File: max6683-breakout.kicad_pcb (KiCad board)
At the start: 2 copper layers, 11 parts, among them J1 Conn_01x05, J2 Conn_01x05, U1 MAX6683

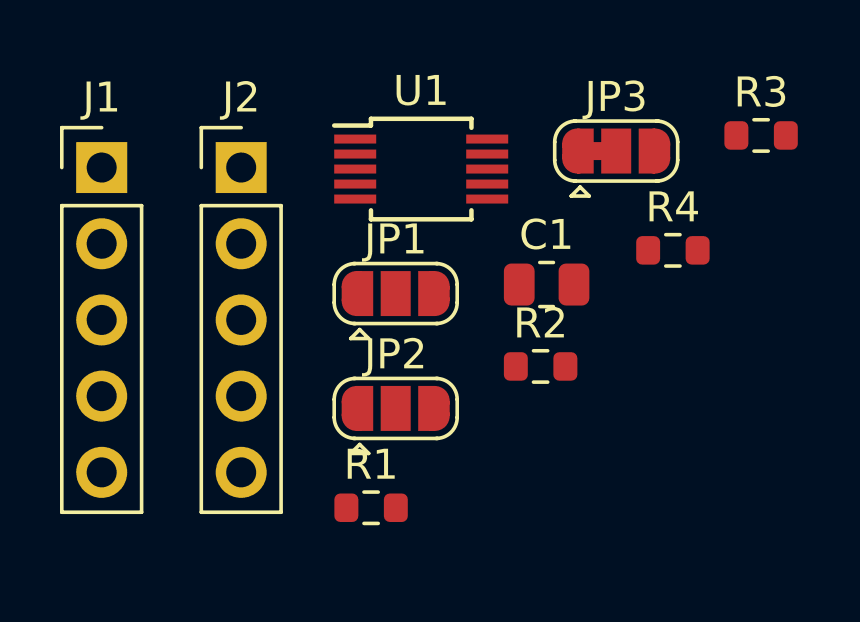
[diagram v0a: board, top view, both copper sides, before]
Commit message: Initial PCB component placement
Supports #44.
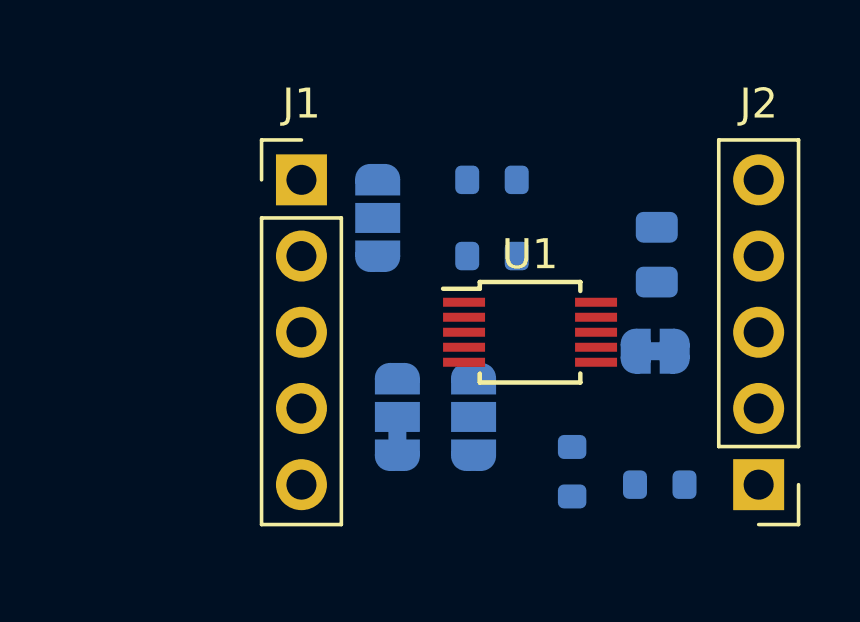
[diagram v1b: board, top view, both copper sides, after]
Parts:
- added JP4: SolderJumper_2_Bridged, Jumper:SolderJumper-2_P1.3mm_Bridged_RoundedPad1.0x1.5mm, B.Cu at (156.6, 102.2)
- C1, JP1, JP2, JP3, R3, R4: moved to B.Cu
- R1, R2: value 4.7k -> 2.2k; moved to B.Cu
- moved J2 20.2 mm to (160.0, 106.7), turned to 180 degrees
- moved R3 12.1 mm to (156.7, 106.7)
- moved R1 11.6 mm to (151.1, 96.5)
- moved JP3 11.5 mm to (148.0, 104.4), turned to 90 degrees
- moved R4 8.11 mm to (153.8, 106.2), turned to -90 degrees
- moved J1 6.67 mm to (144.8, 96.5)
- moved U1 6.54 mm to (152.4, 101.6)
- moved R2 4.02 mm to (151.1, 99.1)
- moved C1 3.80 mm to (156.6, 99.0), turned to 90 degrees
- moved JP2 2.61 mm to (150.5, 104.4), turned to -90 degrees
- moved JP1 2.59 mm to (147.3, 97.8), turned to 90 degrees
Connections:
- J2 pad 1: Net-(U1-Pad6) -> ~{ALERT}
- JP2 pad 1: Net-(JP2-Pad1) -> SCL
- JP2 pad 3: SCL -> Net-(JP2-Pad3)
- JP3 pad 1: SDA -> GND
- JP3 pad 3: GND -> SDA
- R3 pad 1: +3V3 -> Net-(JP4-Pad1)
- R3 pad 2: unconnected-(R3-Pad2) -> ~{ALERT}
- R4 pad 2: Net-(JP2-Pad1) -> Net-(JP2-Pad3)
- U1 pad 6: Net-(U1-Pad6) -> ~{ALERT}

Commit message: Add PCB outline
Parts moved for clearance and ease of routing.

Supports #44.
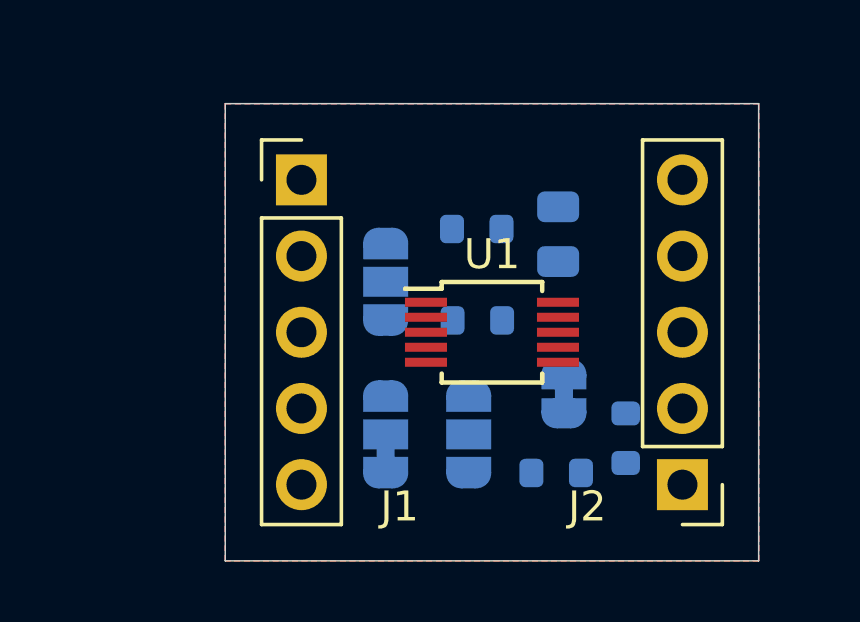
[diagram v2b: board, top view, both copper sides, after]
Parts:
- moved C1 3.36 mm to (153.3, 98.3)
- moved JP4 3.36 mm to (153.5, 103.7), turned to 90 degrees
- moved J2 2.54 mm to (157.5, 106.7)
- moved R2 2.20 mm to (150.6, 101.2)
- moved JP1 2.14 mm to (147.6, 99.9)
- moved R3 1.92 mm to (155.6, 105.1), turned to -90 degrees
- moved R1 1.72 mm to (150.6, 98.2)
- moved U1 1.27 mm to (151.1, 101.6)
- moved JP3 0.70 mm to (147.6, 105.0)
- moved JP2 0.60 mm to (150.4, 105.0)
- moved R4 0.53 mm to (153.3, 106.3), turned to 180 degrees
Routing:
- added copper zone on B.Cu, net +3V3
- added copper zone on F.Cu, net GND
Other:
- board outline added: 17.8 x 15.2 mm

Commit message: Update PCB to eliminate clearance DRC issues
Supports #44.
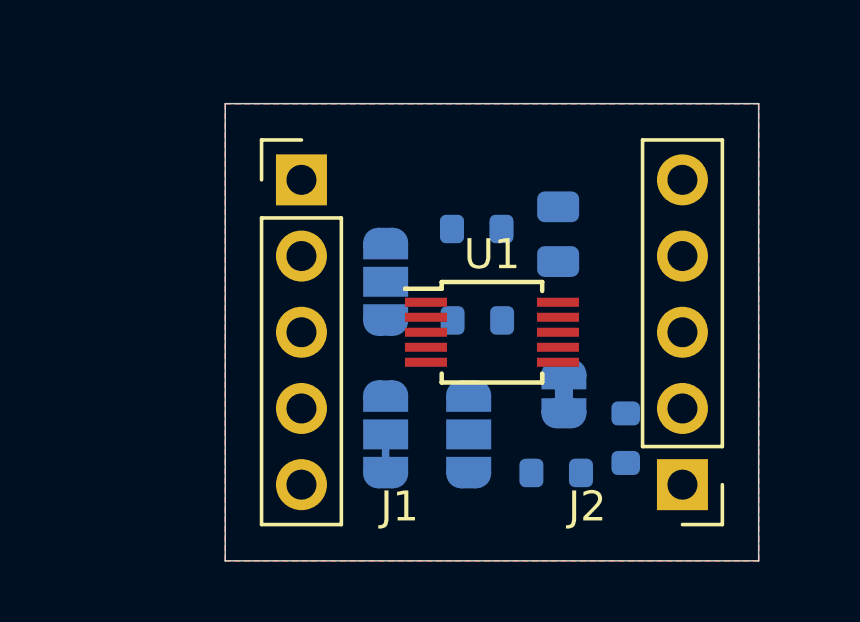
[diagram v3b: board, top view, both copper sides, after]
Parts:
- JP3: footprint Jumper:SolderJumper-3_P1.3mm_Bridged12_RoundedPad1.0x1.5mm -> Jumper:SolderJumper-3_P1.3mm_Open_RoundedPad1.0x1.5mm
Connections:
- C1 pad 2: GND -> ADD
- J1 pad 5: GND -> ADD
- JP3 pad 1: GND -> ADD
- U1 pad 5: GND -> ADD
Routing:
- net ADD: track 0.00 -> 1.30 mm
- added copper zone on F.Cu, net ADD
- removed copper zone on F.Cu, net GND

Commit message: Begin routing
Supports #44.
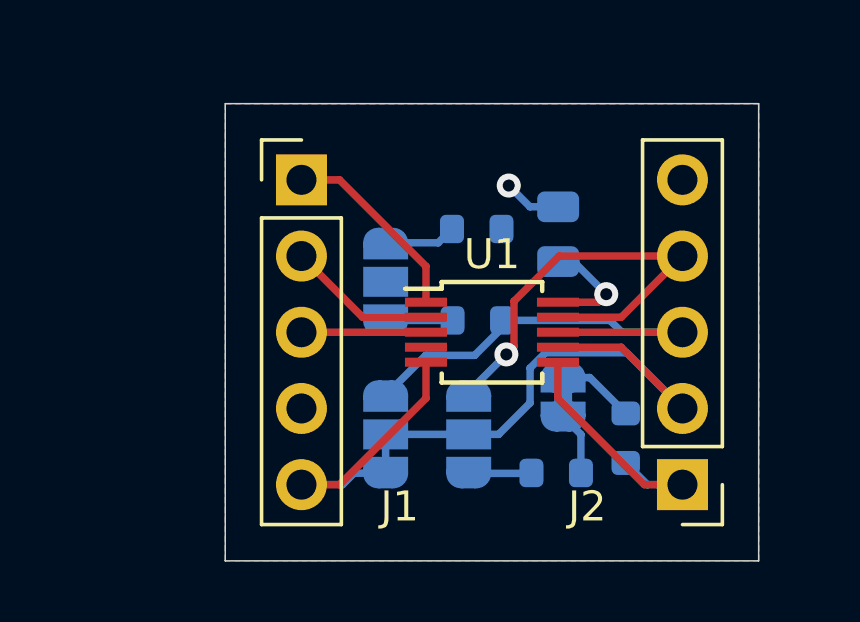
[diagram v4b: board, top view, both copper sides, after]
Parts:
- moved JP4 0.11 mm to (153.5, 103.8), turned to -90 degrees
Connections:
- C1 pad 2: ADD -> GND
- J1 pad 5: ADD -> GND
- JP3 pad 1: ADD -> GND
- U1 pad 5: ADD -> GND
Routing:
- net ADD: track 1.30 -> 18.8 mm
- net SDA: track 0.00 -> 15.4 mm
- net SCL: track 0.00 -> 15.0 mm, vias 0 -> 1
- net GND: track 0.00 -> 11.3 mm, vias 0 -> 1
- net ~{ALERT}: track 0.00 -> 8.73 mm
- net Net-(J1-Pad1): track 0.00 -> 6.54 mm
- net +3V3: track 0.00 -> 6.50 mm, vias 0 -> 1
- net Net-(J1-Pad2): track 0.00 -> 4.99 mm
- net Net-(J1-Pad3): track 0.00 -> 4.15 mm
- net Net-(JP4-Pad1): track 0.00 -> 2.58 mm
- net Net-(JP1-Pad3): track 0.00 -> 2.40 mm
- net Net-(JP1-Pad1): track 0.00 -> 2.24 mm
- net Net-(JP2-Pad3): track 0.00 -> 2.10 mm
- added copper zone on F.Cu, net GND
- removed copper zone on F.Cu, net ADD

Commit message: Complete routing
Supports #44.
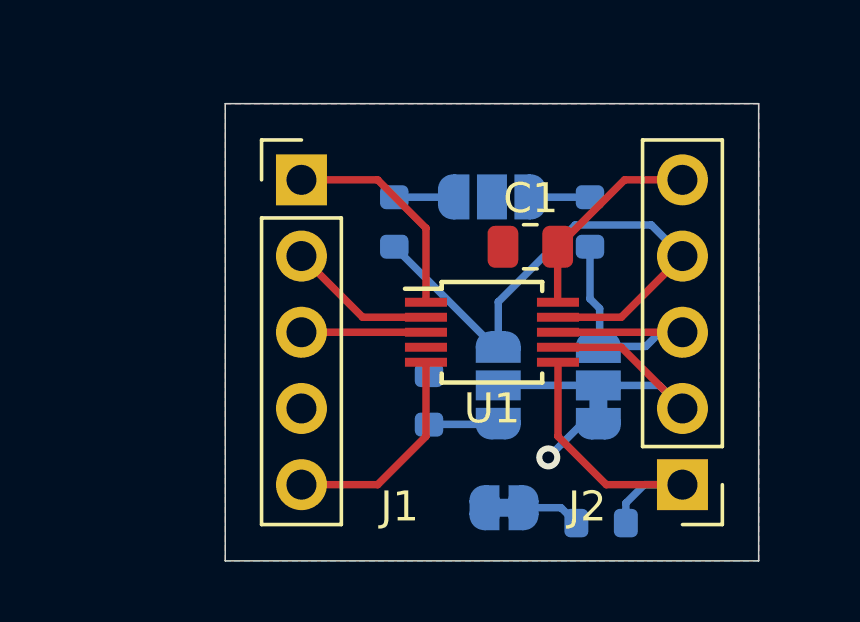
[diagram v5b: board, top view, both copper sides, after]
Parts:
- C1: moved to F.Cu
- JP3: footprint Jumper:SolderJumper-3_P1.3mm_Open_RoundedPad1.0x1.5mm -> Jumper:SolderJumper-3_P1.3mm_Bridged12_RoundedPad1.0x1.5mm_NumberLabels
- moved JP3 7.28 mm to (154.7, 103.4)
- moved R2 4.99 mm to (154.4, 97.9), turned to -90 degrees
- moved R4 4.89 mm to (149.0, 103.9), turned to -90 degrees
- moved JP1 4.54 mm to (151.1, 97.1), turned to 180 degrees
- moved JP4 4.18 mm to (151.5, 107.4), turned to 180 degrees
- moved R3 2.95 mm to (154.8, 108.0), turned to 0 degrees
- moved R1 2.76 mm to (147.9, 97.9), turned to -90 degrees
- moved JP2 1.91 mm to (151.3, 103.4)
- moved C1 1.02 mm to (152.4, 98.8), turned to 180 degrees
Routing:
- net ADD: track 18.8 -> 11.5 mm
- net SDA: track 15.4 -> 10.6 mm
- net SCL: track 15.0 -> 18.9 mm, vias 1 -> 0
- net GND: track 11.3 -> 9.41 mm
- net ~{ALERT}: track 8.73 -> 10.1 mm
- net Net-(J1-Pad1): track 6.54 -> 7.29 mm
- net Net-(JP4-Pad1): track 2.58 -> 1.97 mm
- net +3V3: track 6.50 -> 6.94 mm, vias 1 -> 0
